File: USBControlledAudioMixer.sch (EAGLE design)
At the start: 54 parts, among them IC1 TDA7448, IC2 TS912, IC3 MEGA8-AI, J2 AVR_SPI_PRG_6NS, Q1 16MHz, U1 LMR62014

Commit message: Fixed capacitor order number
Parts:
- C4, C6: OC_TME TAJA155K016R -> T491A106M016AT; PRICE_100 0.059 -> 0.064
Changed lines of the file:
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@@
 </part>
 <part name="C4" library="rcl" deviceset="CPOL-EU" device="SMCA" value="10u">
-<attribute name="OC_TME" value="TAJA155K016R"/>
-<attribute name="PRICE_100" value="0.059"/>
+<attribute name="OC_TME" value="T491A106M016AT"/>
+<attribute name="PRICE_100" value="0.064"/>
 </part>
 <part name="IN3" library="FC68125" deviceset="FC68125" device="">
@@
 </part>
 <part name="C6" library="rcl" deviceset="CPOL-EU" device="SMCA" value="10u">
-<attribute name="OC_TME" value="TAJA155K016R"/>
-<attribute name="PRICE_100" value="0.059"/>
+<attribute name="OC_TME" value="T491A106M016AT"/>
+<attribute name="PRICE_100" value="0.064"/>
 </part>
 <part name="RN2" library="Simplex-rlc" deviceset="RES_ARR" device="" value="1k">

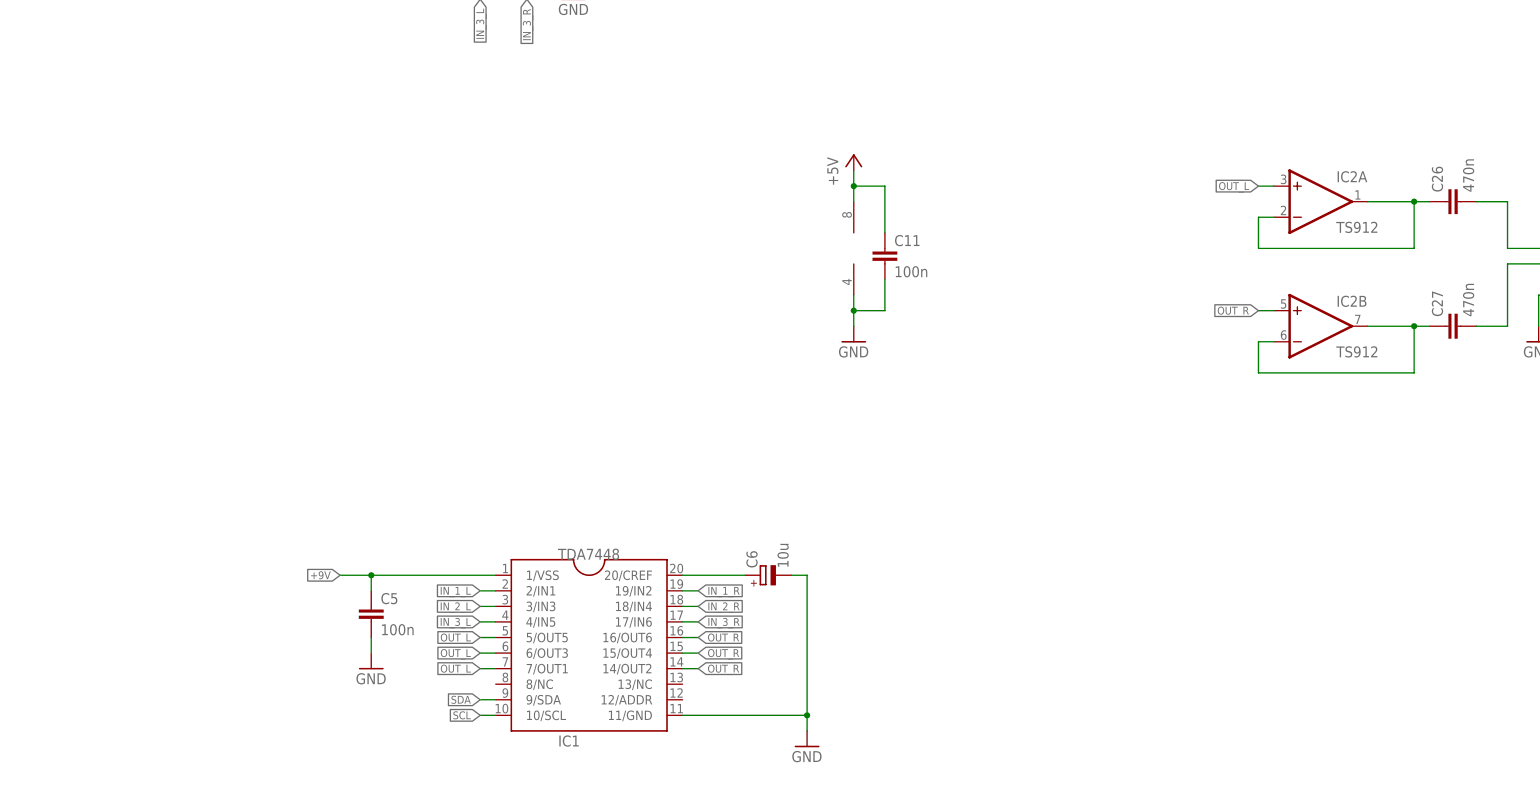
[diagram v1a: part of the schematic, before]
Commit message: Fixed audio mixing
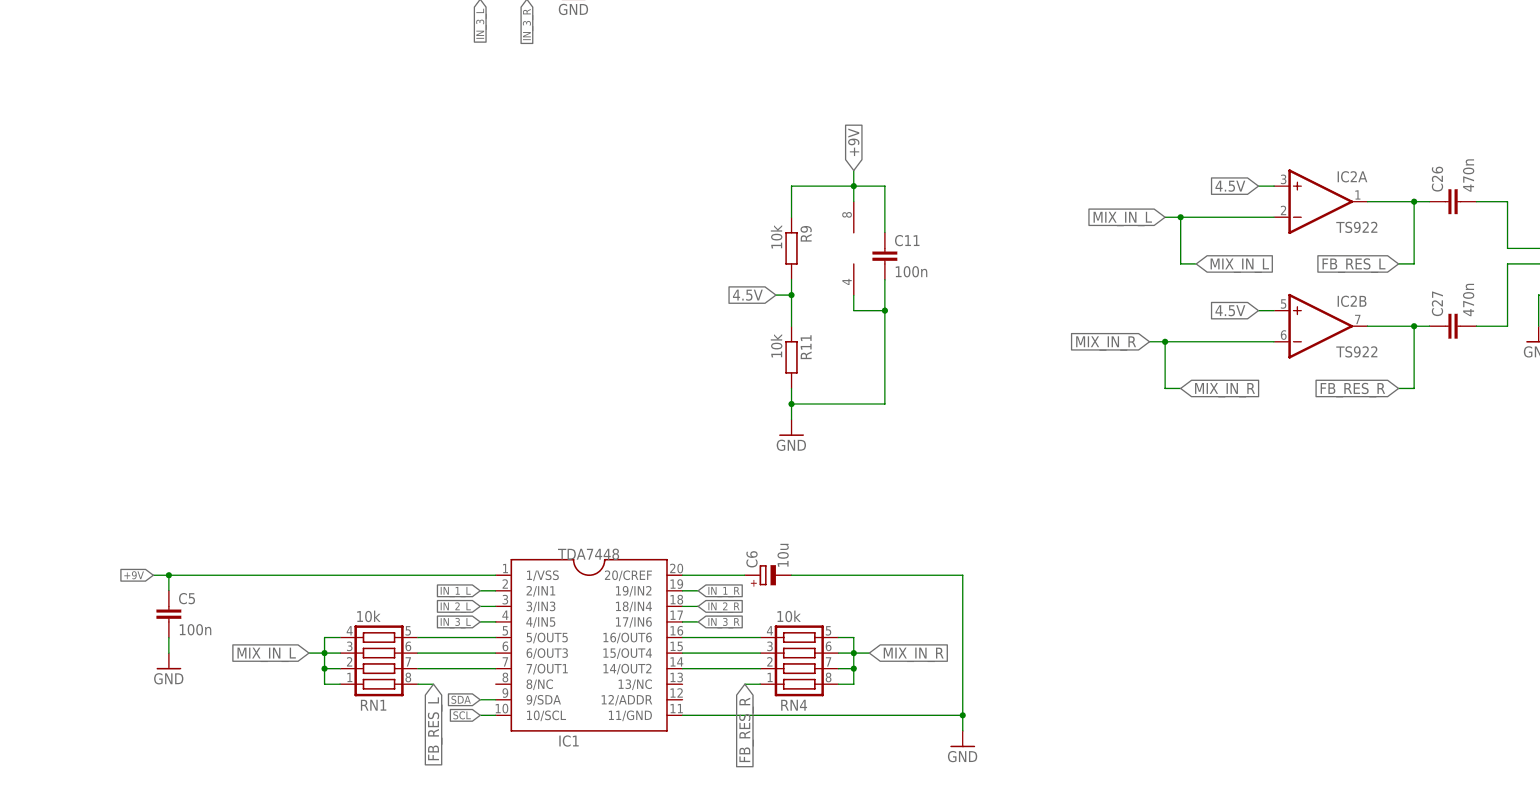
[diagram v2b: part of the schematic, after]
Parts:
- added R11, R9: 10k, rcl:R-EU_R0603
- added RN1, RN4: 10k, Simplex-rlc:RES_ARR
- IC2: value TS912 -> TS922; OC_DIGIKEY 497-6618-1-ND -> 497-6035-1-ND; PRICE_100 0.654 -> 0.546
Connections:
- removed net N$100: C27.1, IC2B.-IN, IC2B.OUT
- removed net N$24: C26.1, IC2A.-IN, IC2A.OUT
- removed net OUT_L: IC1.5/OUT5, IC1.6/OUT3, IC1.7/OUT1, IC2A.+IN
- removed net OUT_R: IC1.14/OUT2, IC1.15/OUT4, IC1.16/OUT6, IC2B.+IN
- new net 4.5V: IC2A.+IN, IC2B.+IN, R11.1, R9.2
- new net FB_RES_L: C26.1, IC2A.OUT, RN1.8
- new net FB_RES_R: C27.1, IC2B.OUT, RN4.1
- new net MIX_IN_L: IC2A.-IN, RN1.1, RN1.2, RN1.3, RN1.4
- new net MIX_IN_R: IC2B.-IN, RN4.5, RN4.6, RN4.7, RN4.8
- new net N$21: IC1.5/OUT5, RN1.5
- new net N$22: IC1.6/OUT3, RN1.6
- new net N$25: IC1.7/OUT1, RN1.7
- new net N$27: IC1.16/OUT6, RN4.4
- new net N$28: IC1.15/OUT4, RN4.3
- new net N$29: IC1.14/OUT2, RN4.2
- net +5V: no longer C11.1, IC2P.V+
- net +9V: now also C11.1, IC2P.V+, R9.1
- net GND: now also R11.2
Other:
- moved on the sheet: C5
